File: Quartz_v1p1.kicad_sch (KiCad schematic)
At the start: 5 parts, among them J1 5747847-6, J2 5747847-6

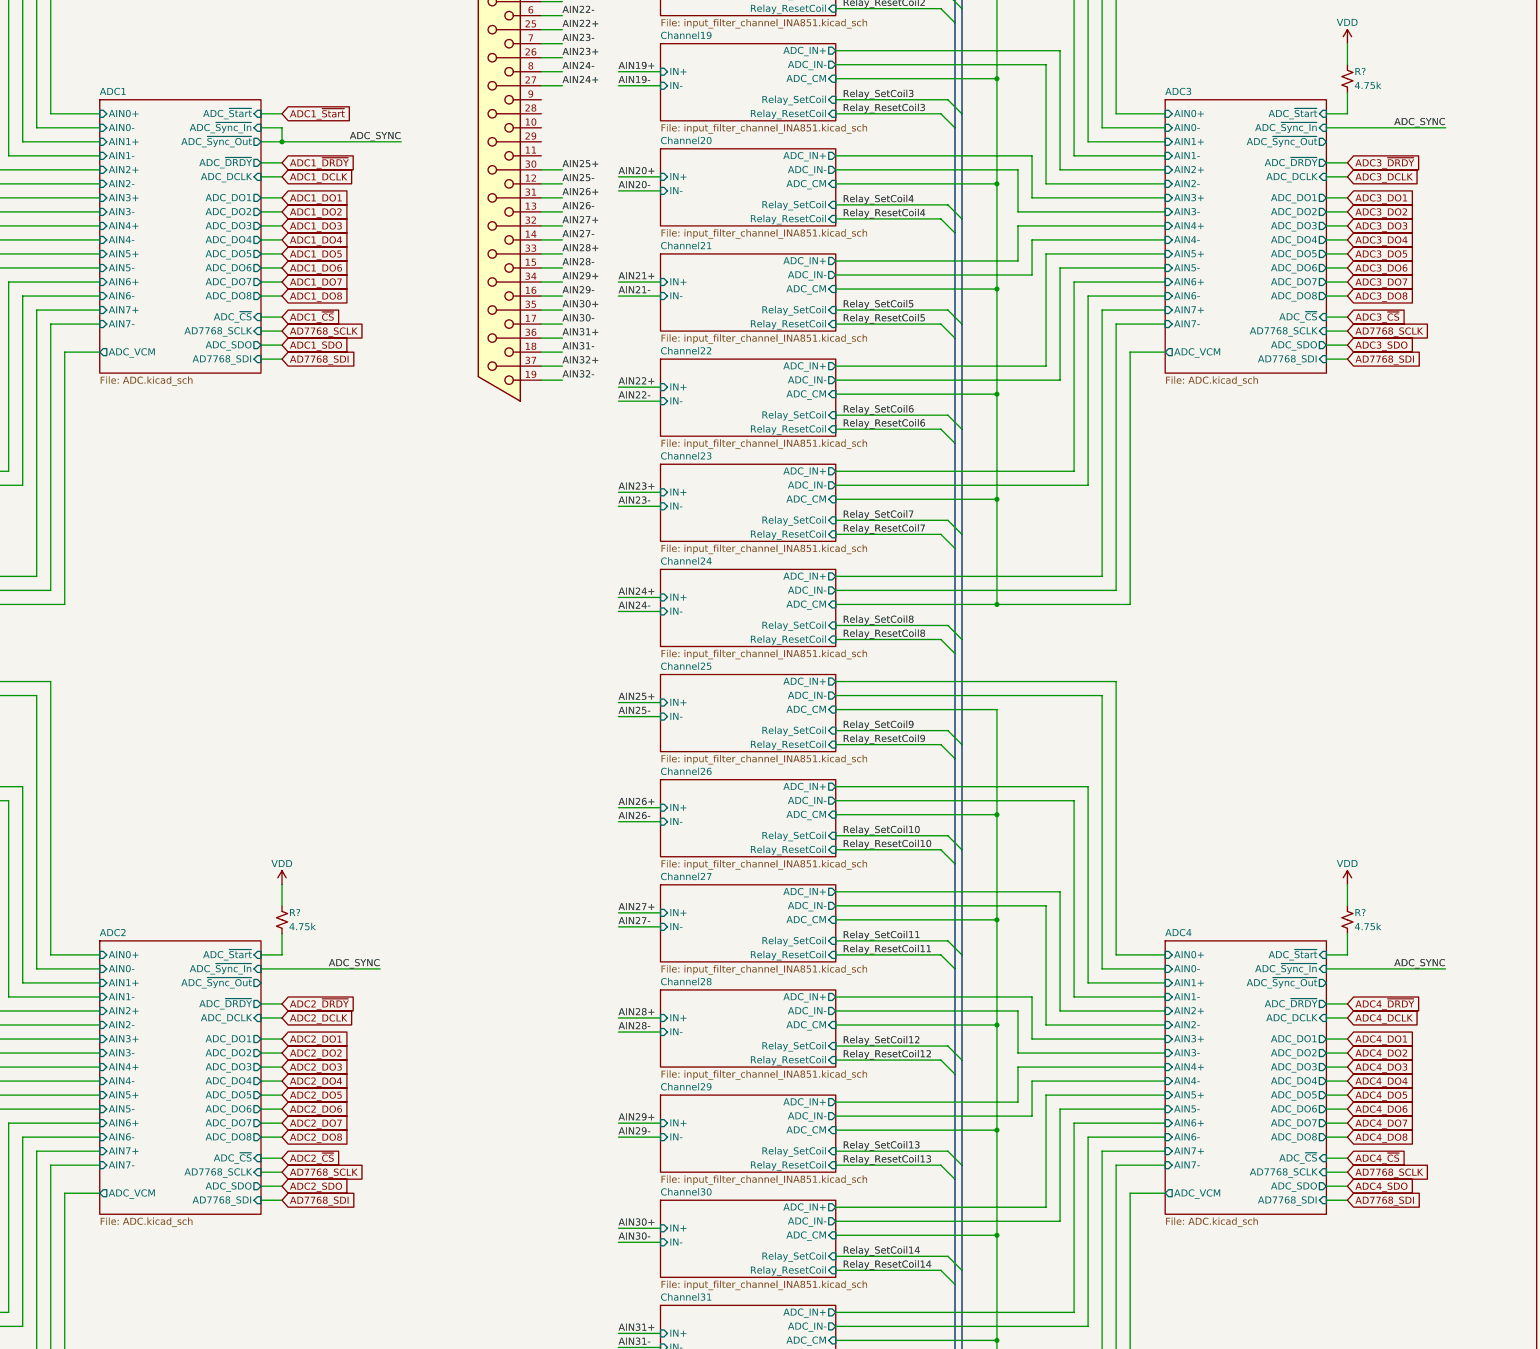
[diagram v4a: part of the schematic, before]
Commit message: Updated Schematics
Changes:
-Moved Input resistors to after Coupling Relay
-Added diff cap at ADC input
-Changed the ADC clocking configuration (added quad LVDS driver)
-Changed some signal names for consistancy
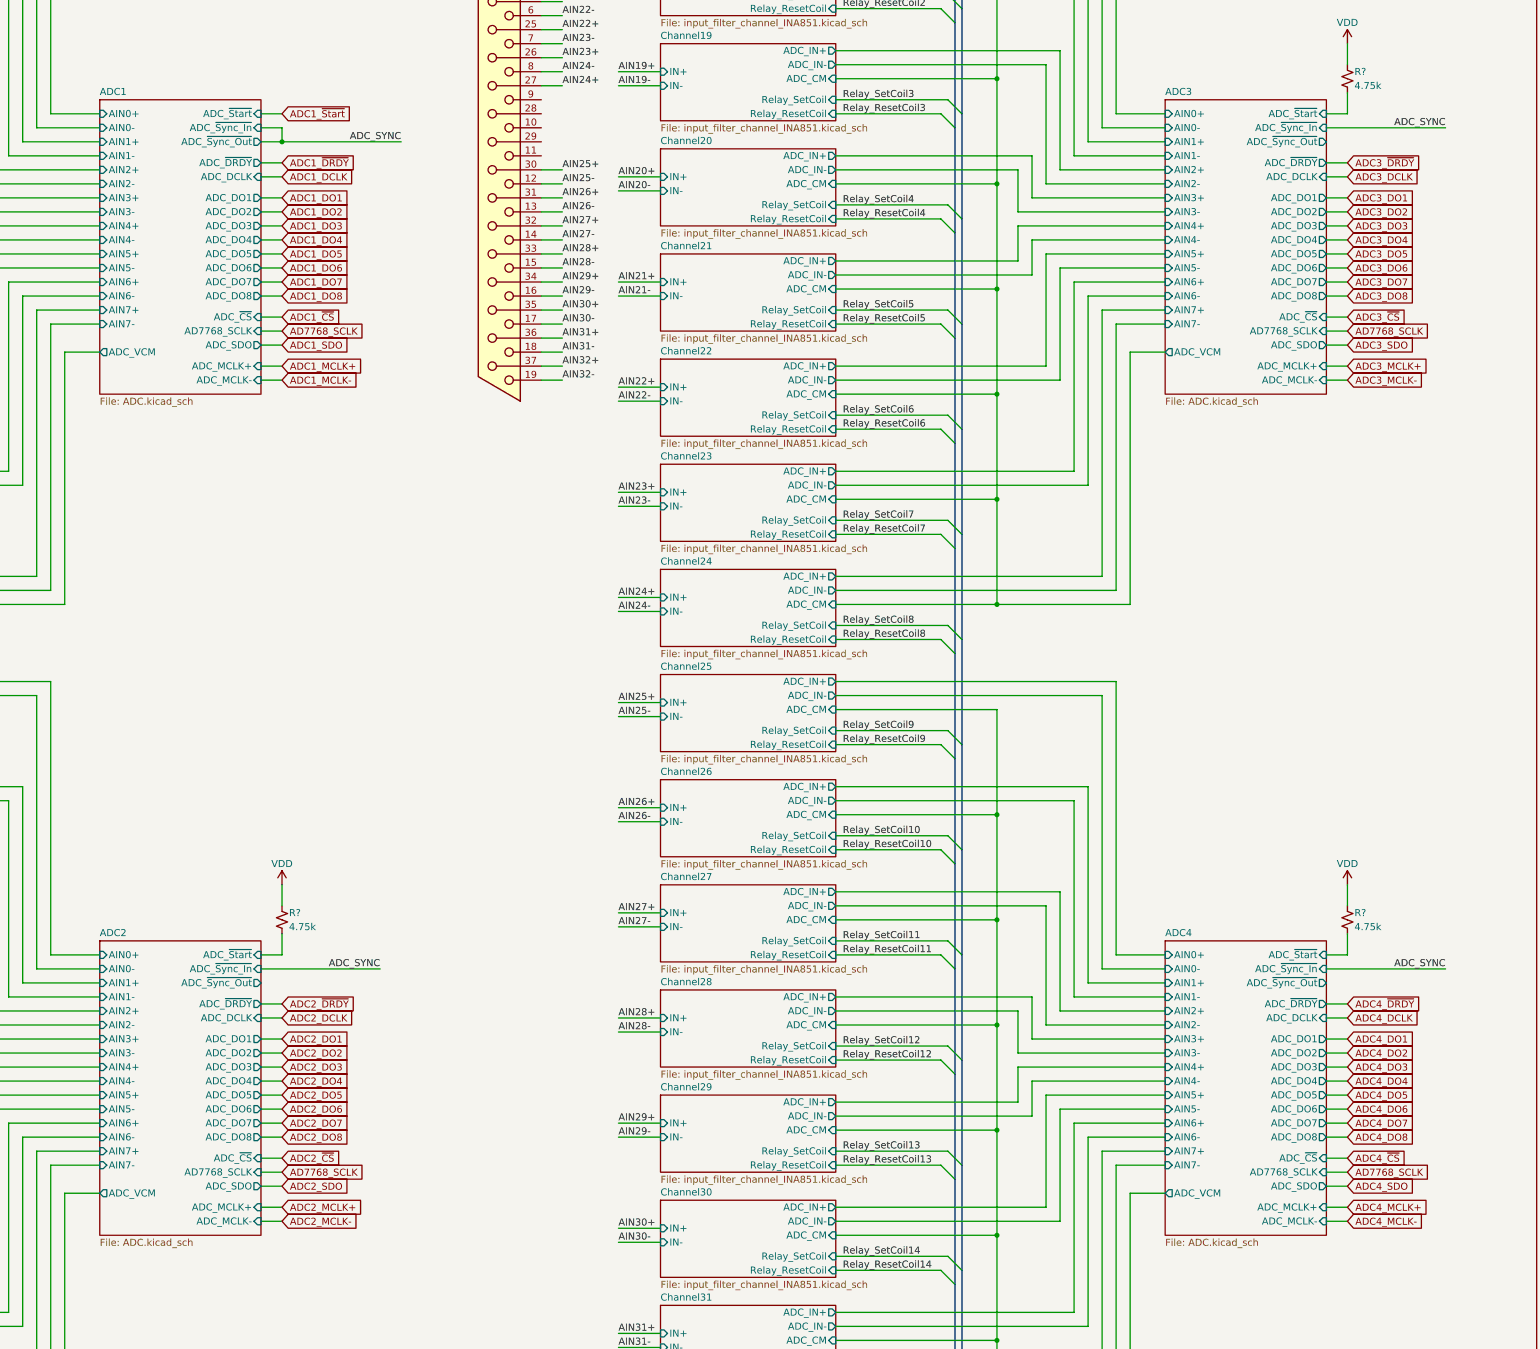
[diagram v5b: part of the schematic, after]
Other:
- sheet ADC1 ports: added ADC_MCLK+, ADC_MCLK-; removed AD7768_SDI
- sheet ADC2 ports: added ADC_MCLK+, ADC_MCLK-; removed AD7768_SDI
- sheet ADC3 ports: added ADC_MCLK+, ADC_MCLK-; removed AD7768_SDI
- sheet ADC4 ports: added ADC_MCLK+, ADC_MCLK-; removed AD7768_SDI

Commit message: Updated Schematic
-Changed PPS input signal buffer
-Made Tweaks to Power Supply section  (Many involving the LT3097) as suggested by Trent.
- general schematic clean up for readability
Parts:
- J1, J2: MPN (none) -> 5747847-6
- R? (x3): footprint (none) -> Resistor_SMD:R_0603_1608Metric; MPN (none) -> RC0603FR-074K75L
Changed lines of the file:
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@@
       (effects (font (size 1.27 1.27)) (justify left))
     )
-    (property "Footprint" "" (at 232.41 220.98 0)
+    (property "Footprint" "Resistor_SMD:R_0603_1608Metric" (at 232.41 220.98 0)
       (effects (font (size 1.27 1.27)) hide)
     )
     (property "Datasheet" "~" (at 232.41 220.98 0)
+      (effects (font (size 1.27 1.27)) hide)
+    )
+    (property "MPN" "RC0603FR-074K75L" (at 232.41 220.98 0)
       (effects (font (size 1.27 1.27)) hide)
     )
@@
         )
         (path "/674e1e7f-67ba-4e85-a926-dcd5f6a22021"
-          (reference "R4001") (unit 1)
+          (reference "R1") (unit 1)
         )
       )
@@
       (effects (font (size 1.27 1.27)) (justify left))
     )
-    (property "Footprint" "" (at 425.45 220.98 0)
+    (property "Footprint" "Resistor_SMD:R_0603_1608Metric" (at 425.45 220.98 0)
       (effects (font (size 1.27 1.27)) hide)
     )
     (property "Datasheet" "~" (at 425.45 220.98 0)
+      (effects (font (size 1.27 1.27)) hide)
+    )
+    (property "MPN" "RC0603FR-074K75L" (at 425.45 220.98 0)
       (effects (font (size 1.27 1.27)) hide)
     )
@@
         )
         (path "/674e1e7f-67ba-4e85-a926-dcd5f6a22021"
-          (reference "R4003") (unit 1)
+          (reference "R3") (unit 1)
         )
       )
@@
         )
         (path "/674e1e7f-67ba-4e85-a926-dcd5f6a22021"
-          (reference "#PWR04001") (unit 1)
+          (reference "#PWR01") (unit 1)
         )
       )
@@
       (effects (font (size 1.27 1.27)) (justify left))
     )
-    (property "Footprint" "" (at 425.45 68.58 0)
+    (property "Footprint" "Resistor_SMD:R_0603_1608Metric" (at 425.45 68.58 0)
       (effects (font (size 1.27 1.27)) hide)
     )
     (property "Datasheet" "~" (at 425.45 68.58 0)
+      (effects (font (size 1.27 1.27)) hide)
+    )
+    (property "MPN" "RC0603FR-074K75L" (at 425.45 68.58 0)
       (effects (font (size 1.27 1.27)) hide)
     )
@@
         )
         (path "/674e1e7f-67ba-4e85-a926-dcd5f6a22021"
-          (reference "R4002") (unit 1)
+          (reference "R2") (unit 1)
         )
       )
@@
     (property "Datasheet" "" (at 276.86 80.01 0)
       (effects (font (size 1.27 1.27) italic) hide)
+    )
+    (property "MPN" "5747847-6" (at 271.78 77.47 0)
+      (effects (font (size 1.27 1.27)) hide)
     )
     (pin "1")
@@
       (project "Quartz_v1p1"
         (path "/674e1e7f-67ba-4e85-a926-dcd5f6a22021"
-          (reference "J4002") (unit 1)
+          (reference "J2") (unit 1)
         )
       )
@@
         )
         (path "/674e1e7f-67ba-4e85-a926-dcd5f6a22021"
-          (reference "#PWR04003") (unit 1)
+          (reference "#PWR03") (unit 1)
         )
       )
@@
     (property "Datasheet" "" (at 85.09 81.28 0)
       (effects (font (size 1.27 1.27) italic) hide)
+    )
+    (property "MPN" "5747847-6" (at 80.01 78.74 0)
+      (effects (font (size 1.27 1.27)) hide)
     )
     (pin "1")
@@
       (project "Quartz_v1p1"
         (path "/674e1e7f-67ba-4e85-a926-dcd5f6a22021"
-          (reference "J4001") (unit 1)
+          (reference "J1") (unit 1)
         )
       )
@@
         )
         (path "/674e1e7f-67ba-4e85-a926-dcd5f6a22021"
-          (reference "#PWR04002") (unit 1)
-        )
-      )
+          (reference "#PWR02") (unit 1)
+        )
+      )
